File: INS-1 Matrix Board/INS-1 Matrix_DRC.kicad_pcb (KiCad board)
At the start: 2 copper layers, 49.4 x 116.2 mm, 134 parts, among them J1 Conn_02x04_Odd_Even, J2 Conn_02x04_Odd_Even, T0 INS-1, T1 INS-1, T10 INS-1, T11 INS-1, T12 INS-1, T13 INS-1, T14 INS-1, T15 INS-1, T16 INS-1, T17 INS-1, T18 INS-1, T19 INS-1, T2 INS-1, T20 INS-1, T21 INS-1, T22 INS-1, T23 INS-1, T24 INS-1, T25 INS-1, T26 INS-1, T27 INS-1, T28 INS-1, T29 INS-1, T3 INS-1, T30 INS-1, T31 INS-1, T32 INS-1, T33 INS-1, T34 INS-1, T35 INS-1, T36 INS-1, T37 INS-1, T38 INS-1, T39 INS-1, T4 INS-1, T40 INS-1, T41 INS-1, T42 INS-1, T43 INS-1, T44 INS-1, T45 INS-1, T46 INS-1, T47 INS-1, T48 INS-1, T49 INS-1, T5 INS-1, T50 INS-1, T51 INS-1, T52 INS-1, T53 INS-1, T54 INS-1, T55 INS-1, T56 INS-1, T57 INS-1, T58 INS-1, T59 INS-1, T6 INS-1, T7 INS-1, T8 INS-1, T9 INS-1, U1 HV5530, U2 HV5530

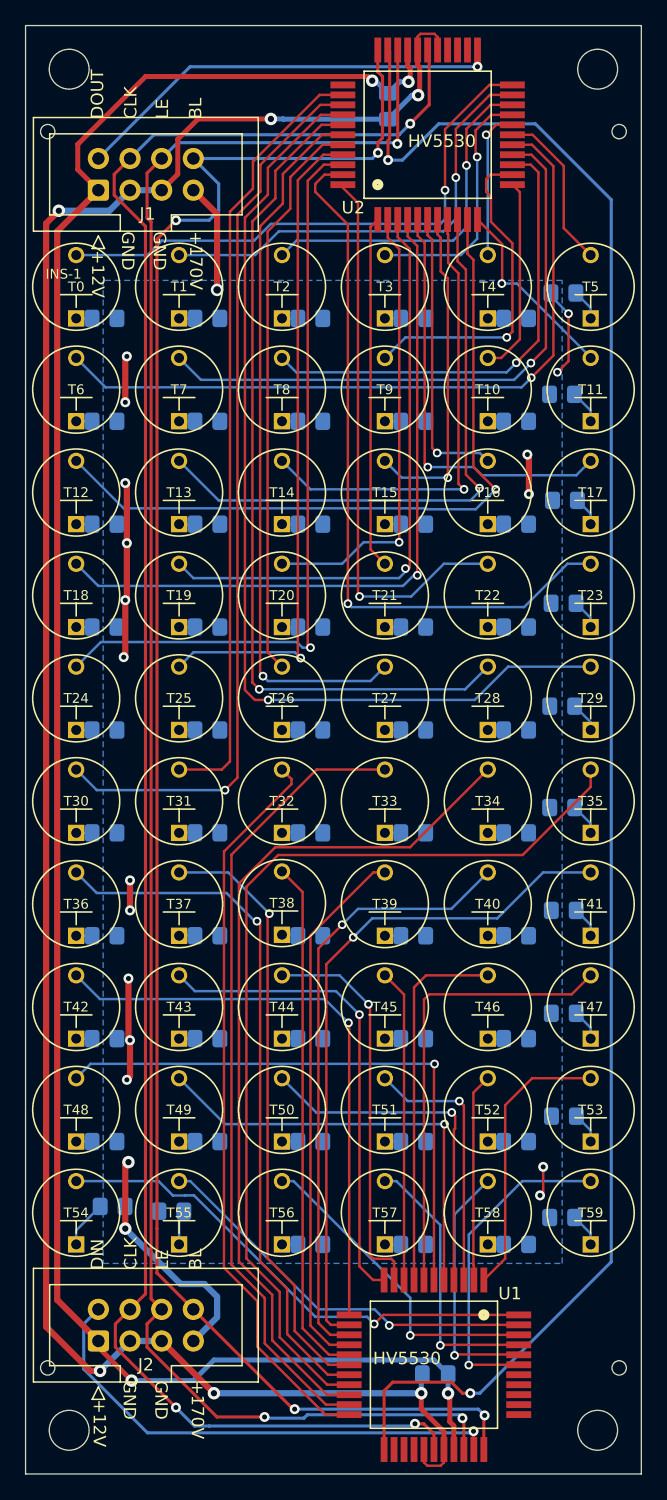
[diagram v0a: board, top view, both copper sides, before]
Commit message: Change POL pin to connect to 12V
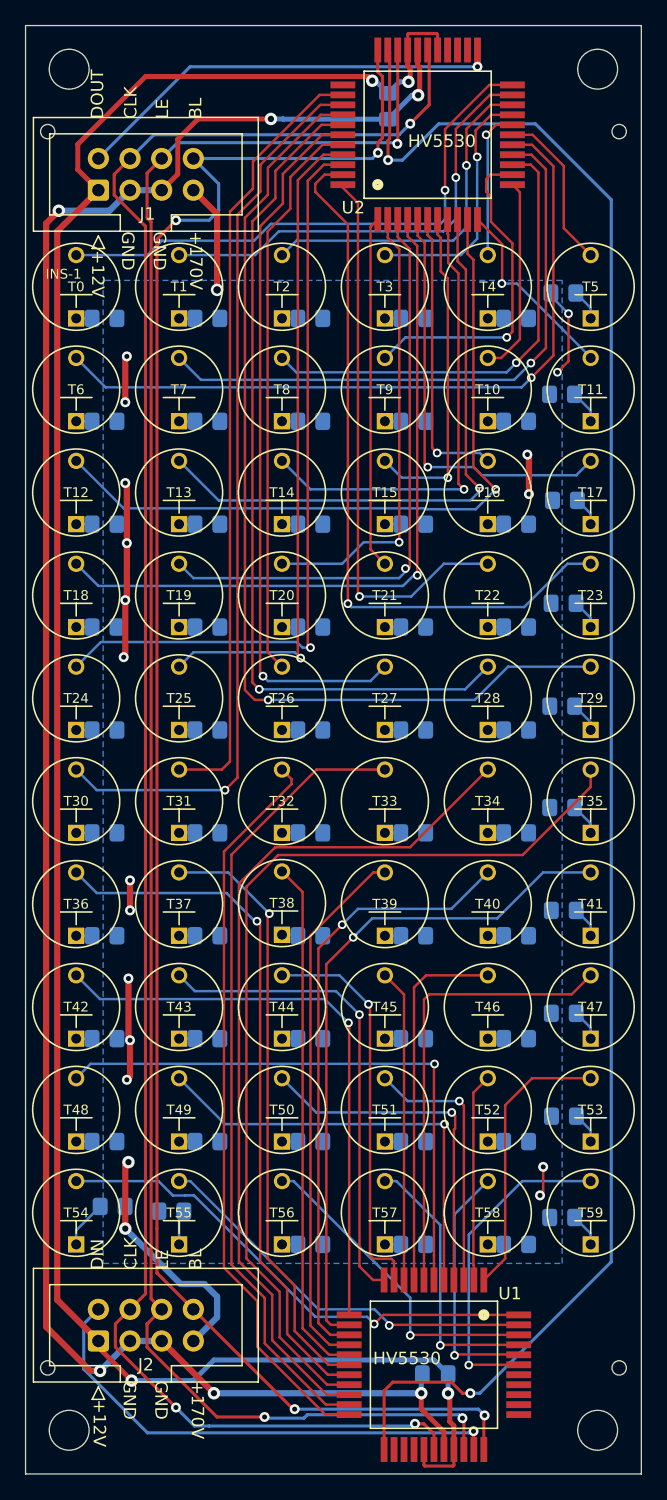
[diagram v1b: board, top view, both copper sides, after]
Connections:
- U1 pad POL: GND -> +12V
- U2 pad POL: GND -> +12V
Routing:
- net +12V: track 168.9 -> 178.8 mm
- net GND: track 177.0 -> 169.1 mm
